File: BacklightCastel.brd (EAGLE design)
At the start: 15 x 14.2 mm, 7 parts, among them U1 TLV61046A

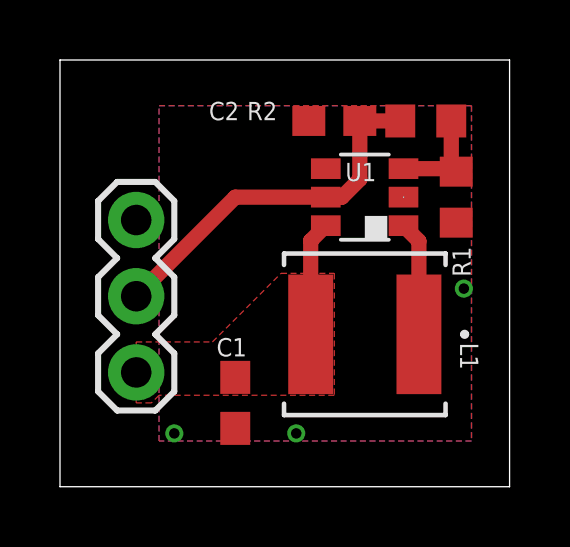
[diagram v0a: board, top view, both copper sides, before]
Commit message: Layout update
Moved output capacitor, swapped R1 & R2, tied EN to VCC
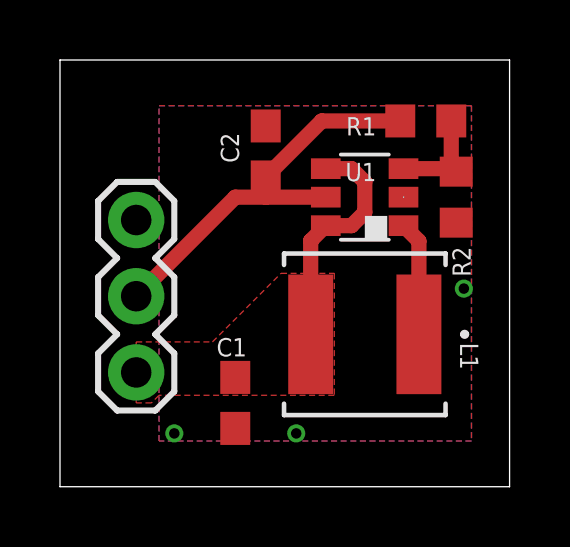
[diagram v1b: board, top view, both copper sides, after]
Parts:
- L1: value NRS5020T220MMGJ -> 22uH
- R1: value 71.5k -> 1.65M
- R2: value 1.65M -> 71.5k
- moved R1 2.74 mm to (12.2, 12.2), turned to 0 degrees
- moved R2 2.74 mm to (13.2, 9.65), turned to 270 degrees
- moved C2 2.50 mm to (6.86, 11.2), turned to 90 degrees
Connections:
- net FB: now also R1.2, R2.1; no longer R1.1, R2.2
- net GND: now also R2.2; no longer R1.2
- net OUT: now also R1.1; no longer R2.1
- net VCC: now also U1.4
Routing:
- net VCC: track 3.83 -> 7.81 mm
- net OUT: track 12.4 -> 13.6 mm
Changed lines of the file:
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@@
 </autorouter>
 <elements>
-<element name="C2" library="rcl" library_urn="urn:adsk.eagle:library:334" package="C0603" package3d_urn="urn:adsk.eagle:package:23616/2" value="1uF" x="9.144" y="12.192" smashed="yes" rot="R180">
-<attribute name="NAME" x="5.969" y="12.827" size="0.6096" layer="25" font="vector" ratio="20" rot="R180"/>
-<attribute name="SPICEPREFIX" value="C" x="-7.366" y="35.052" size="1.778" layer="27" rot="R180" display="off"/>
-<attribute name="VALUE" x="9.779" y="14.097" size="1.27" layer="27" rot="R180"/>
+<element name="C2" library="rcl" library_urn="urn:adsk.eagle:library:334" package="C0603" package3d_urn="urn:adsk.eagle:package:23616/2" value="1uF" x="6.858" y="11.176" smashed="yes" rot="R90">
+<attribute name="NAME" x="5.969" y="10.795" size="0.6096" layer="25" font="vector" ratio="20" rot="R90"/>
+<attribute name="SPICEPREFIX" value="C" x="29.718" y="27.686" size="1.778" layer="27" rot="R90" display="off"/>
+<attribute name="VALUE" x="8.763" y="10.541" size="1.27" layer="27" rot="R90"/>
 </element>
 <element name="C1" library="rcl" library_urn="urn:adsk.eagle:library:334" package="C0603" package3d_urn="urn:adsk.eagle:package:23616/2" value="4.7uF" x="5.842" y="2.794" smashed="yes" rot="R90">
@@
 <attribute name="VALUE" x="0.508" y="10.16" size="0.6096" layer="27" font="vector" ratio="20" rot="R270"/>
 </element>
-<element name="L1" library="dsl" package="IND_TAIYO_NRS5020" value="NRS5020T220MMGJ" x="10.16" y="5.08" smashed="yes" rot="R180">
+<element name="L1" library="dsl" package="IND_TAIYO_NRS5020" value="22uH" x="10.16" y="5.08" smashed="yes" rot="R180">
 <attribute name="MANUFACTURER_PART_NUMBER" value="NRS5020T220MMGJ" x="-6.35" y="16.51" size="1.778" layer="27" rot="R180" display="off"/>
 <attribute name="NAME" x="13.335" y="4.8006" size="0.6096" layer="25" font="vector" ratio="20" rot="SR270"/>
 <attribute name="VENDOR" value="TAIYO YUDEN" x="-6.35" y="16.51" size="1.778" layer="27" rot="R180" display="off"/>
 </element>
-<element name="R2" library="resistor" library_urn="urn:adsk.eagle:library:348" package="R0603" package3d_urn="urn:adsk.eagle:package:23555/2" value="1.65M" x="12.192" y="12.192" smashed="yes">
-<attribute name="NAME" x="7.239" y="12.827" size="0.6096" layer="25" font="vector" ratio="20" rot="R180"/>
+<element name="R1" library="resistor" library_urn="urn:adsk.eagle:library:348" package="R0603" package3d_urn="urn:adsk.eagle:package:23555/2" value="1.65M" x="12.192" y="12.192" smashed="yes">
+<attribute name="NAME" x="10.541" y="12.319" size="0.6096" layer="25" font="vector" ratio="20" rot="R180"/>
 <attribute name="VALUE" x="11.557" y="10.287" size="1.27" layer="27"/>
 </element>
-<element name="R1" library="resistor" library_urn="urn:adsk.eagle:library:348" package="R0603" package3d_urn="urn:adsk.eagle:package:23555/2" value="71.5k" x="13.208" y="9.652" smashed="yes" rot="R270">
+<element name="R2" library="resistor" library_urn="urn:adsk.eagle:library:348" package="R0603" package3d_urn="urn:adsk.eagle:package:23555/2" value="71.5k" x="13.208" y="9.652" smashed="yes" rot="R270">
 <attribute name="NAME" x="13.081" y="8.001" size="0.6096" layer="25" font="vector" ratio="20" rot="R270"/>
 <attribute name="VALUE" x="11.303" y="10.287" size="1.27" layer="27" rot="R270"/>
@@
 <contactref element="U1" pad="2"/>
 <contactref element="C1" pad="1"/>
-<contactref element="R1" pad="2"/>
+<contactref element="R2" pad="2"/>
 <contactref element="C2" pad="2"/>
 <contactref element="J1" pad="1"/>
@@
 <wire x1="8.3566" y1="5.08" x2="8.3566" y2="8.1986" width="0.508" layer="1"/>
 <wire x1="8.3566" y1="8.1986" x2="8.86" y2="8.702" width="0.508" layer="1"/>
+<contactref element="U1" pad="4"/>
+<wire x1="8.86" y1="10.602" x2="9.718" y2="10.602" width="0.508" layer="1"/>
+<wire x1="9.718" y1="10.602" x2="10.16" y2="10.16" width="0.508" layer="1"/>
+<wire x1="10.16" y1="10.16" x2="10.16" y2="9.144" width="0.508" layer="1"/>
+<wire x1="10.16" y1="9.144" x2="9.718" y2="8.702" width="0.508" layer="1"/>
+<wire x1="9.718" y1="8.702" x2="8.86" y2="8.702" width="0.508" layer="1"/>
+<wire x1="5.842" y1="3.644" x2="8.3566" y2="5.08" width="0" layer="19" extent="1-1"/>
+<wire x1="2.54" y1="3.81" x2="5.842" y2="3.644" width="0" layer="19" extent="1-1"/>
 </signal>
 <signal name="SW">
@@
 </signal>
 <signal name="FB">
-<contactref element="R2" pad="2"/>
-<contactref element="R1" pad="1"/>
+<contactref element="R1" pad="2"/>
+<contactref element="R2" pad="1"/>
 <contactref element="U1" pad="3"/>
 <wire x1="11.45" y1="10.602" x2="13.108" y2="10.602" width="0.508" layer="1"/>
@@
 </signal>
 <signal name="OUT">
-<contactref element="R2" pad="1"/>
+<contactref element="R1" pad="1"/>
 <contactref element="U1" pad="5"/>
 <contactref element="C2" pad="1"/>
 <contactref element="J1" pad="2"/>
 <wire x1="2.54" y1="6.35" x2="5.842" y2="9.652" width="0.508" layer="1"/>
-<wire x1="5.842" y1="9.652" x2="8.86" y2="9.652" width="0.508" layer="1"/>
-<wire x1="8.86" y1="9.652" x2="9.398" y2="9.652" width="0.508" layer="1"/>
-<wire x1="9.398" y1="9.652" x2="9.994" y2="10.248" width="0.508" layer="1"/>
-<wire x1="9.994" y1="10.248" x2="9.994" y2="12.192" width="0.508" layer="1"/>
-<wire x1="11.342" y1="12.192" x2="9.994" y2="12.192" width="0.508" layer="1"/>
+<wire x1="5.842" y1="9.652" x2="6.858" y2="9.652" width="0.508" layer="1"/>
+<wire x1="6.858" y1="9.652" x2="8.86" y2="9.652" width="0.508" layer="1"/>
+<wire x1="6.858" y1="10.326" x2="6.858" y2="9.652" width="0.508" layer="1"/>
+<wire x1="8.724" y1="12.192" x2="6.858" y2="10.326" width="0.508" layer="1"/>
+<wire x1="11.342" y1="12.192" x2="8.724" y2="12.192" width="0.508" layer="1"/>
 </signal>
 </signals>
